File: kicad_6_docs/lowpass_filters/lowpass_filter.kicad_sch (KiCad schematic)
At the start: 48 parts, among them Q10 BCM847, Q11 BCM847, Q12 BCM847, Q13 BCM847, Q14 BCM847, Q15 BCM847, Q16 BCM847, Q17 MMBT3906, Q18 MMBT3904, U1 TL072

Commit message: Initial filter board layout
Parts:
- C19, C22, C23, C24: value 22n -> 22n 2.5%
- R64: value 47k -> 100k
- RV10: value 1k -> 10k
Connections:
- net +5VA is gone; now on net +15V: RV12.1
- net at C18.1, C19.2, Q10.4 (E): now also Q11.6 (C); no longer Q11.3 (C)
- net at C22.2, Q12.3 (C): now also Q11.1 (E); no longer Q11.4 (E)
- net at C22.1, Q12.6 (C): now also Q11.4 (E); no longer Q11.1 (E)
- net at C19.1, C20.1, Q10.1 (E): now also Q11.3 (C); no longer Q11.6 (C)
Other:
- moved on the sheet: Q11A, Q11B
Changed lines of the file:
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@@
     (in_bom yes) (on_board yes) (fields_autoplaced)
     (property "Reference" "C23" (id 0) (at 120.65 97.79 90))
-    (property "Value" "22n" (id 1) (at 120.65 100.33 90))
+    (property "Value" "22n 2.5%" (id 1) (at 120.65 100.33 90))
     (property "Footprint" "Capacitor_THT:C_Rect_L7.2mm_W7.2mm_P5.00mm_FKS2_FKP2_MKS2_MKP2" (id 2) (at 124.46 104.4448 0)
       (effects (font (size 1.27 1.27)) hide)
@@
     (pin "1")
   )
-  (symbol (lib_id "custom_symbols:BCM847DS135") (at 130.81 76.2 0) (mirror y) (unit 2)
-    (in_bom yes) (on_board yes)
-    (property "Reference" "Q11" (id 0) (at 135.89 69.85 0)
-      (effects (font (size 1.27 1.27)) (justify left))
-    )
-    (property "Value" "BCM847" (id 1) (at 139.7 72.39 0)
-      (effects (font (size 1.27 1.27)) (justify left))
-    )
-    (property "Footprint" "custom_footprints:SOT457" (id 2) (at 135.89 78.105 0)
-      (effects (font (size 1.27 1.27) italic) (justify left) hide)
-    )
-    (property "Datasheet" "" (id 3) (at 130.81 76.2 0)
+  (symbol (lib_id "custom_symbols:BCM847DS135") (at 110.49 76.2 0) (unit 2)
+    (in_bom yes) (on_board yes)
+    (property "Reference" "Q11" (id 0) (at 105.41 69.85 0)
+      (effects (font (size 1.27 1.27)) (justify left))
+    )
+    (property "Value" "BCM847" (id 1) (at 101.6 72.39 0)
+      (effects (font (size 1.27 1.27)) (justify left))
+    )
+    (property "Footprint" "custom_footprints:SOT457" (id 2) (at 105.41 78.105 0)
+      (effects (font (size 1.27 1.27) italic) (justify left) hide)
+    )
+    (property "Datasheet" "" (id 3) (at 110.49 76.2 0)
       (effects (font (size 1.27 1.27)) (justify left) hide)
     )
@@
     (pin "2")
   )
-  (symbol (lib_id "custom_symbols:BCM847DS135") (at 110.49 76.2 0) (unit 1)
-    (in_bom yes) (on_board yes)
-    (property "Reference" "Q11" (id 0) (at 102.87 69.85 0)
-      (effects (font (size 1.27 1.27)) (justify left))
-    )
-    (property "Value" "BCM847" (id 1) (at 102.87 72.39 0)
-      (effects (font (size 1.27 1.27)) (justify left))
-    )
-    (property "Footprint" "custom_footprints:SOT457" (id 2) (at 105.41 78.105 0)
-      (effects (font (size 1.27 1.27) italic) (justify left) hide)
-    )
-    (property "Datasheet" "" (id 3) (at 110.49 76.2 0)
+  (symbol (lib_id "custom_symbols:BCM847DS135") (at 130.81 76.2 0) (mirror y) (unit 1)
+    (in_bom yes) (on_board yes)
+    (property "Reference" "Q11" (id 0) (at 138.43 69.85 0)
+      (effects (font (size 1.27 1.27)) (justify left))
+    )
+    (property "Value" "BCM847" (id 1) (at 138.43 72.39 0)
+      (effects (font (size 1.27 1.27)) (justify left))
+    )
+    (property "Footprint" "custom_footprints:SOT457" (id 2) (at 135.89 78.105 0)
+      (effects (font (size 1.27 1.27) italic) (justify left) hide)
+    )
+    (property "Datasheet" "" (id 3) (at 130.81 76.2 0)
       (effects (font (size 1.27 1.27)) (justify left) hide)
     )
@@
     (in_bom yes) (on_board yes) (fields_autoplaced)
     (property "Reference" "C22" (id 0) (at 120.65 76.2 90))
-    (property "Value" "22n" (id 1) (at 120.65 78.74 90))
+    (property "Value" "22n 2.5%" (id 1) (at 120.65 78.74 90))
     (property "Footprint" "Capacitor_THT:C_Rect_L7.2mm_W7.2mm_P5.00mm_FKS2_FKP2_MKS2_MKP2" (id 2) (at 124.46 82.8548 0)
       (effects (font (size 1.27 1.27)) hide)
@@
     (in_bom yes) (on_board yes) (fields_autoplaced)
     (property "Reference" "R64" (id 0) (at 97.79 176.53 90))
-    (property "Value" "47k" (id 1) (at 97.79 179.07 90))
+    (property "Value" "100k" (id 1) (at 97.79 179.07 90))
     (property "Footprint" "Resistor_SMD:R_0805_2012Metric" (id 2) (at 97.79 184.658 90)
       (effects (font (size 1.27 1.27)) hide)
@@
   (symbol (lib_id "Device:C") (at 120.65 57.15 90) (unit 1)
     (in_bom yes) (on_board yes)
-    (property "Reference" "C19" (id 0) (at 120.65 46.99 90))
-    (property "Value" "22n" (id 1) (at 120.65 52.07 90))
+    (property "Reference" "C19" (id 0) (at 120.65 49.53 90))
+    (property "Value" "22n 2.5%" (id 1) (at 120.65 52.07 90))
     (property "Footprint" "Capacitor_THT:C_Rect_L7.2mm_W7.2mm_P5.00mm_FKS2_FKP2_MKS2_MKP2" (id 2) (at 124.46 56.1848 0)
       (effects (font (size 1.27 1.27)) hide)
@@
       (effects (font (size 1.27 1.27)) (justify right))
     )
-    (property "Value" "1k" (id 1) (at 147.32 139.6999 0)
+    (property "Value" "10k" (id 1) (at 147.32 139.6999 0)
       (effects (font (size 1.27 1.27)) (justify right))
     )
@@
     (pin "4")
     (pin "5")
+  )
+  (symbol (lib_id "power:+15V") (at 87.63 176.53 0) (unit 1)
+    (in_bom yes) (on_board yes) (fields_autoplaced)
+    (property "Reference" "#PWR?" (id 0) (at 87.63 180.34 0)
+      (effects (font (size 1.27 1.27)) hide)
+    )
+    (property "Value" "+15V" (id 1) (at 87.63 171.45 0))
+    (property "Footprint" "" (id 2) (at 87.63 176.53 0)
+      (effects (font (size 1.27 1.27)) hide)
+    )
+    (property "Datasheet" "" (id 3) (at 87.63 176.53 0)
+      (effects (font (size 1.27 1.27)) hide)
+    )
+    (pin "1")
   )
   (symbol (lib_id "power:GND") (at 140.97 170.18 0) (unit 1)
@@
     (pin "5")
   )
-  (symbol (lib_id "power:+5VA") (at 87.63 176.53 0) (unit 1)
-    (in_bom yes) (on_board yes) (fields_autoplaced)
-    (property "Reference" "#PWR018" (id 0) (at 87.63 180.34 0)
-      (effects (font (size 1.27 1.27)) hide)
-    )
-    (property "Value" "+5VA" (id 1) (at 87.63 171.45 0))
-    (property "Footprint" "" (id 2) (at 87.63 176.53 0)
-      (effects (font (size 1.27 1.27)) hide)
-    )
-    (property "Datasheet" "" (id 3) (at 87.63 176.53 0)
-      (effects (font (size 1.27 1.27)) hide)
-    )
-    (pin "1")
-  )
   (symbol (lib_id "power:-15V") (at 194.31 96.52 180) (unit 1)
     (in_bom yes) (on_board yes) (fields_autoplaced)
@@
     (in_bom yes) (on_board yes) (fields_autoplaced)
     (property "Reference" "C24" (id 0) (at 120.65 119.38 90))
-    (property "Value" "22n" (id 1) (at 120.65 121.92 90))
+    (property "Value" "22n 2.5%" (id 1) (at 120.65 121.92 90))
     (property "Footprint" "Capacitor_THT:C_Rect_L7.2mm_W7.2mm_P5.00mm_FKS2_FKP2_MKS2_MKP2" (id 2) (at 124.46 126.0348 0)
       (effects (font (size 1.27 1.27)) hide)

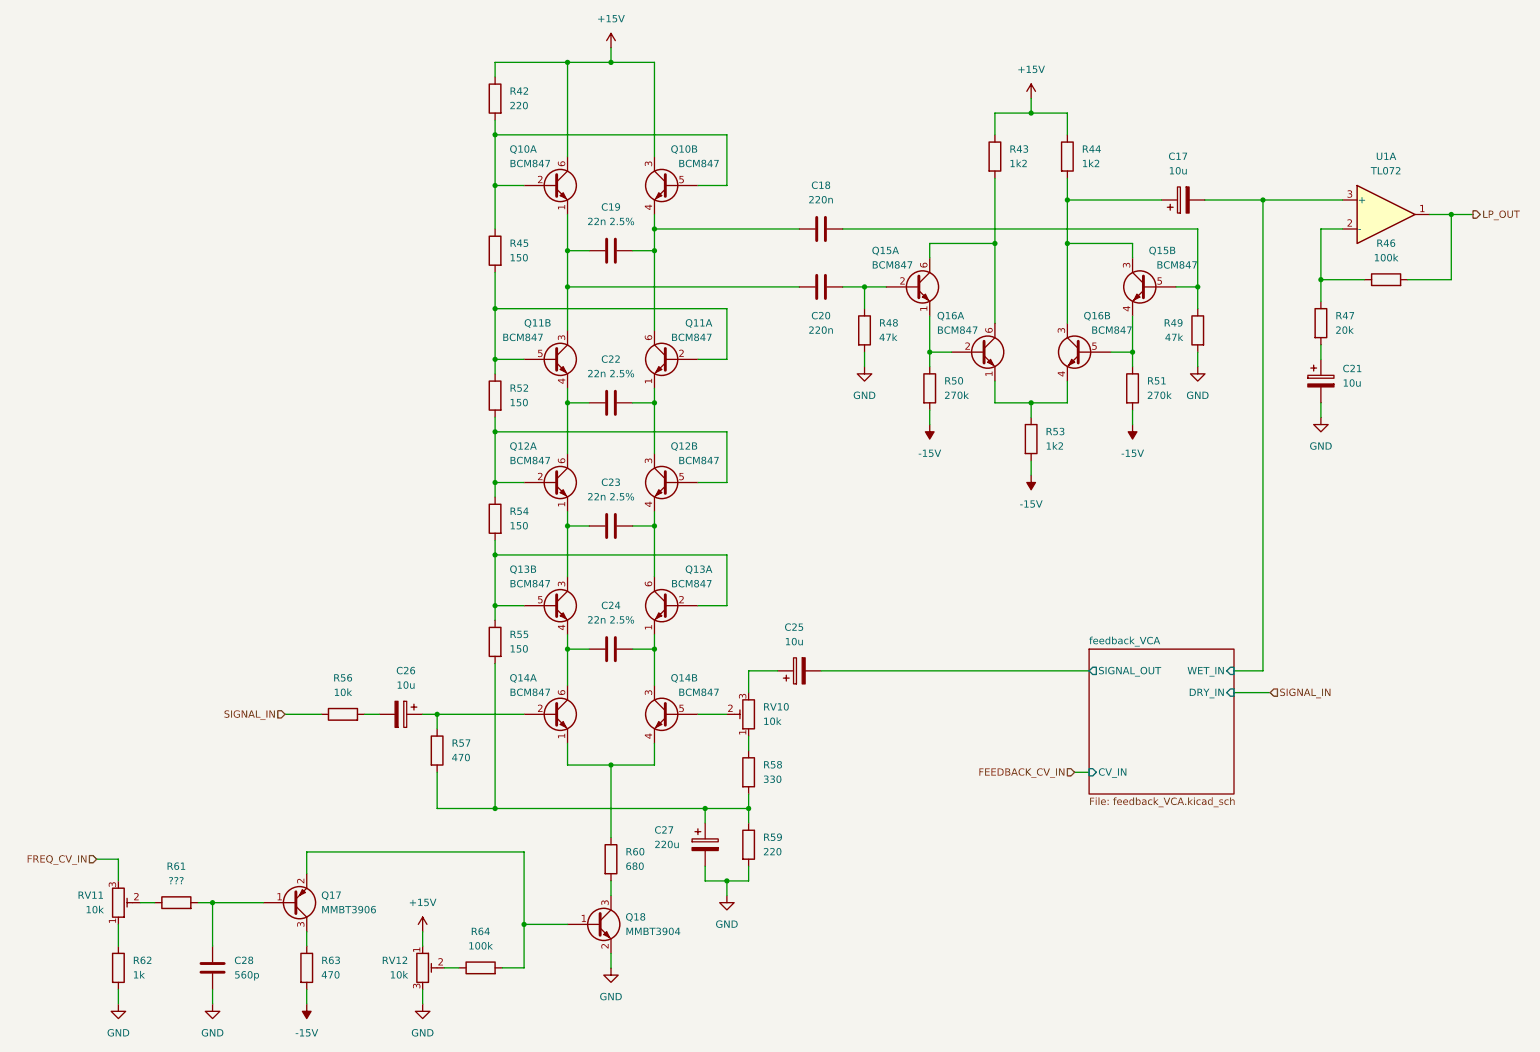
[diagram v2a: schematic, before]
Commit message: Tweak some filter board values
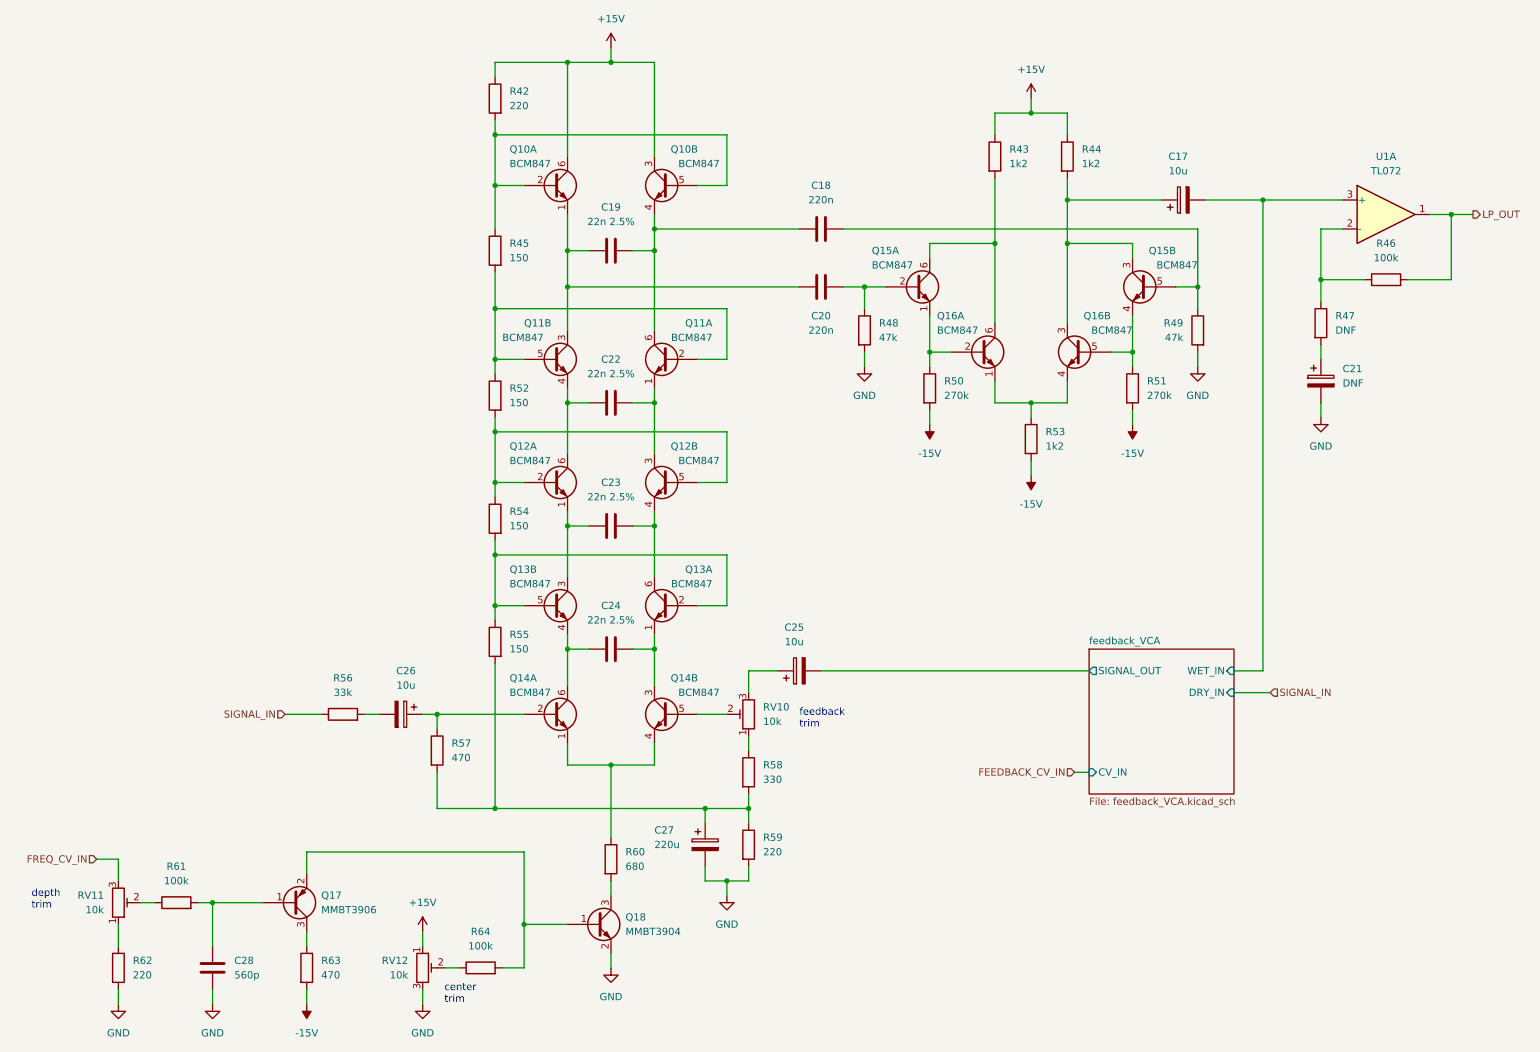
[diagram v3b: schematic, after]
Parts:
- C21: value 10u -> DNF
- R47: value 20k -> DNF
- R56: value 10k -> 33k
- R61: value ??? -> 100k
- R62: value 1k -> 220
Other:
- note added: "center trim"
- note added: "depth trim"
- note added: "feedback trim"
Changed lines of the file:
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@@
   (title_block
     (title "M.S.M. Stereo Lowpass Filter Pedal")
-    (date "2022-05-24")
+    (date "2022-06-16")
     (rev "0")
     (comment 2 "creativecommons.org/licenses/by/4.0")
@@
     (stroke (width 0) (type default) (color 0 0 0 0))
   )
+  (text "feedback\ntrim" (at 153.67 140.97 0)
+    (effects (font (size 1.27 1.27)) (justify left bottom))
+  )
+  (text "center\ntrim" (at 91.44 189.23 0)
+    (effects (font (size 1.27 1.27)) (justify left bottom))
+  )
+  (text "depth\ntrim" (at 19.05 172.72 0)
+    (effects (font (size 1.27 1.27)) (justify left bottom))
+  )
   (hierarchical_label "FREQ_CV_IN" (shape input) (at 30.48 163.83 180)
     (effects (font (size 1.27 1.27)) (justify right))
@@
     (in_bom yes) (on_board yes) (fields_autoplaced)
     (property "Reference" "R56" (id 0) (at 73.66 132.08 90))
-    (property "Value" "10k" (id 1) (at 73.66 134.62 90))
+    (property "Value" "33k" (id 1) (at 73.66 134.62 90))
     (property "Footprint" "Resistor_SMD:R_0805_2012Metric" (id 2) (at 73.66 140.208 90)
       (effects (font (size 1.27 1.27)) hide)
@@
       (effects (font (size 1.27 1.27)) (justify left))
     )
-    (property "Value" "20k" (id 1) (at 247.65 71.1199 0)
+    (property "Value" "DNF" (id 1) (at 247.65 71.1199 0)
       (effects (font (size 1.27 1.27)) (justify left))
     )
@@
       (effects (font (size 1.27 1.27)) (justify left))
     )
-    (property "Value" "1k" (id 1) (at 36.83 184.1499 0)
+    (property "Value" "220" (id 1) (at 36.83 184.1499 0)
       (effects (font (size 1.27 1.27)) (justify left))
     )
@@
     (in_bom yes) (on_board yes) (fields_autoplaced)
     (property "Reference" "R61" (id 0) (at 44.45 165.1 90))
-    (property "Value" "???" (id 1) (at 44.45 167.64 90))
+    (property "Value" "100k" (id 1) (at 44.45 167.64 90))
     (property "Footprint" "Resistor_SMD:R_0805_2012Metric" (id 2) (at 44.45 173.228 90)
       (effects (font (size 1.27 1.27)) hide)
@@
       (effects (font (size 1.27 1.27)) (justify left))
     )
-    (property "Value" "10u" (id 1) (at 248.92 80.3909 0)
-      (effects (font (size 1.27 1.27)) (justify left))
-    )
+    (property "Value" "DNF" (id 1) (at 248.92 80.3909 0)
+      (effects (font (size 1.27 1.27)) (justify left))
+    )
